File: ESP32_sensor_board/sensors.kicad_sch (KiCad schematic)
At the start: 0 parts

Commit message: Schematic design section 3 completed
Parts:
- added C15, C16, C18, C20: 0.1u, Capacitor_SMD:C_0805_2012Metric, symbol Device:C
- added MK1: CMC-5042PF-AC, footprints:CUI_CMC-5042PF-AC, symbol CMC-5042PF-AC:CMC-5042PF-AC
- added Q1: TEMT6000X01, footprints:TRANS_TEMT6000X01, symbol TEMT6000X01:TEMT6000X01
- added R23, R30: 10K, Resistor_SMD:R_0805_2012Metric, symbol Device:R
- added R24, R25: 4K7, Resistor_SMD:R_0805_2012Metric, symbol Device:R
- added R26, R28: 2K, Resistor_SMD:R_0805_2012Metric, symbol Device:R
- added R27, R29: 1M, Resistor_SMD:R_0805_2012Metric, symbol Device:R
- added R31: 100K, Resistor_SMD:R_0805_2012Metric, symbol Device:R
- added U2: BME280, footprints:PSON65P250X250X100-8N, symbol BME280:BME280
- added U7: MAX4466EXK, footprints:SOT65P210X110-5N, symbol MAX4466EXK:MAX4466EXK
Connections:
- new net +3.3V: C15.1, C18.1, R23.1, R24.1, R25.1, R26.1, R27.1, U2.2 (CSB), U2.6 (VDDIO), U2.8 (VDD), U7.5 (VCC)
- new net BIAS: C16.2, R26.2, R28.1
- new net FEEDBACK: C20.1, R30.1, R31.1, U7.3 (IN-)
- new net GND: C15.2, C16.1, C18.2, MK1.GND, Q1.1, R29.2, R30.2, U2.1 (GND), U2.5 (SDO), U2.7 (GND), U7.2 (GND)
- new net MIC_OUT: C20.2, R31.2, U7.4 (OUT)
- new net MK_INPUT: MK1.OUT, R27.2, R28.2, R29.1, U7.1 (IN+)
- new net PHOTO_C: Q1.3, R23.2
- new net SCL: R24.2, U2.4 (SCK)
- new net SDA: R25.2, U2.3 (SDI)
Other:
- note added: "BME280"
- note added: "Microphone and amplifier"
- note added: "PHOTO SENSOR"
- title: (none) -> Sensors

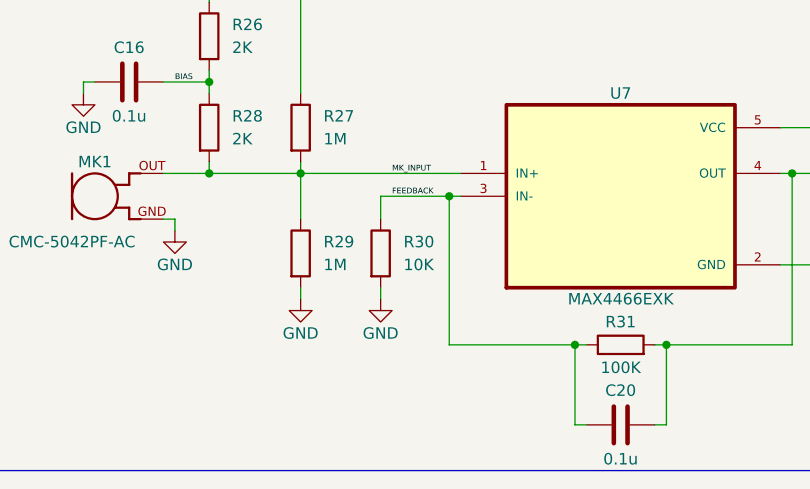
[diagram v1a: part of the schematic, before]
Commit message: Schematic design C19 added
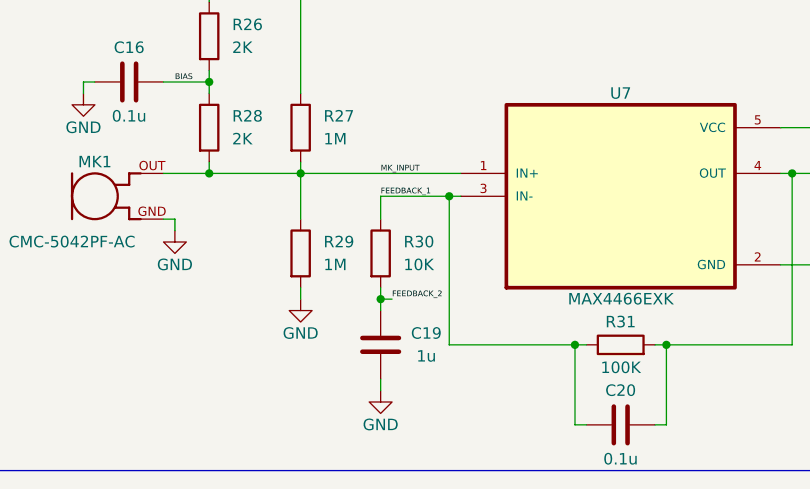
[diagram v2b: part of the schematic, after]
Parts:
- added C19: 1u, Capacitor_SMD:C_0805_2012Metric, symbol Device:C
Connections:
- net GND: now also C19.2; no longer R30.2
- net FEEDBACK renamed FEEDBACK_1
- new net FEEDBACK_2: C19.1, R30.2

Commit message: Layout design section 2 completed
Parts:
- added C17: 10n, Capacitor_SMD:C_0805_2012Metric, symbol Device:C
- C20: value 0.1u -> 100p
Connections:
- net MK_INPUT renamed MK_DC
- net MK_DC: now also C17.2; no longer MK1.OUT, R28.2
- new net MK: C17.1, MK1.OUT, R28.2
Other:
- moved on the sheet: C16, C18, C19, C20, MK1, R26, R27, R28, R29, R30, R31, U7

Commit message: Prototype 2 completed
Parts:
- added C23: 0.1u, Capacitor_SMD:C_0805_2012Metric, symbol Device:C
- added C24, C25: 10n, Capacitor_SMD:C_0805_2012Metric, symbol Device:C
- added R17: 35WR100KLFTR, footprints:TRIM_35WR100KLFTR, symbol 35WR100KLFTR:35WR100KLFTR
- C19: value 1u -> 10u
- C20: value 100p -> 0.1u
- R30: value 10K -> 1K
- R31: value 100K -> 22K
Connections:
- net +3.3V: now also Q1.3, C23.2; no longer R23.1
- net GND: now also R23.2, C23.1, C24.1, C25.1; no longer Q1.1
- net MIC_OUT: now also R17.1, R17.2; no longer R31.2
- net PHOTO_C: now also Q1.1, R23.1, C24.2, C25.2; no longer Q1.3, R23.2
- new net FEEDBACK_3: R17.3, R31.2
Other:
- moved on the sheet: C16, C17, C18, C19, C20, MK1, Q1, R23, R26, R27, R28, R29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
